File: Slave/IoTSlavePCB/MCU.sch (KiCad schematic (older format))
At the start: 12 parts

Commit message: Continued work on slaves. Added sensor and begun work on ZigBee transceiver.
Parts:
- C? (x5): footprint (none) -> Capacitor_SMD:C_0603_1608Metric
- R?: footprint (none) -> Resistor_SMD:R_0603_1608Metric
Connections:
- net JTCK: now also U?.49 (PA14)
- net JTDI: now also U?.50 (PA15)
- net JTDO: now also U?.54 (PB3)
- net JTMS: now also U?.46 (PA13)
- net NRST: now also U?.55 (PB4)
- net USART_RX: now also U?.58 (PB7)
- net USART_TX: now also U?.57 (PB6)
- net SPI1_SCK: now reaches U?.15 (PA1)
- net ~SPI1_NSS: now reaches U?.20 (PA4)
- net SPI1_MISO: now reaches U?.22 (PA6)
- net SPI1_MOSI: now reaches U?.23 (PA7)
- net I2C1_SCL: now reaches U?.42 (PA9)
- net I2C1_SDA: now reaches U?.43 (PA10)
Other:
- moved on the sheet: C?, R?
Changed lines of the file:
@@
 F 0 "C?" H 2250 2550 50  0000 L CNN
 F 1 "100 nF" H 2100 2450 50  0000 L CNN
-F 2 "" H 2538 2300 50  0001 C CNN
+F 2 "Capacitor_SMD:C_0603_1608Metric" H 2538 2300 50  0001 C CNN
 F 3 "~" H 2500 2450 50  0001 C CNN
 	1    2500 2450
@@
 	-1   0    0    1
 $EndComp
-Wire Wire Line
-	2650 3850 2150 3850
 $Comp
 L Device:C C?
 U 1 1 5F9FADD1
-P 2150 4050
-F 0 "C?" H 2150 4150 50  0000 L CNN
-F 1 "1 µF" H 2150 3950 50  0000 L CNN
-F 2 "" H 2188 3900 50  0001 C CNN
-F 3 "~" H 2150 4050 50  0001 C CNN
-	1    2150 4050
+P 2000 4050
+F 0 "C?" H 2000 4150 50  0000 L CNN
+F 1 "1 µF" H 2000 3950 50  0000 L CNN
+F 2 "" H 2038 3900 50  0001 C CNN
+F 3 "~" H 2000 4050 50  0001 C CNN
+	1    2000 4050
 	1    0    0    -1
 $EndComp
@@
 L Device:C C?
 U 1 1 5F9FB54A
-P 1950 4050
-F 0 "C?" H 1850 4150 50  0000 L CNN
-F 1 "10 nF" H 1700 3950 50  0000 L CNN
-F 2 "" H 1988 3900 50  0001 C CNN
-F 3 "~" H 1950 4050 50  0001 C CNN
-	1    1950 4050
-	1    0    0    -1
-$EndComp
-Wire Wire Line
-	2150 3850 2150 3900
-Wire Wire Line
-	2150 3850 1950 3850
-Wire Wire Line
-	1950 3850 1950 3900
-Connection ~ 2150 3850
-Connection ~ 1950 3850
+P 1800 4050
+F 0 "C?" H 1700 4150 50  0000 L CNN
+F 1 "10 nF" H 1550 3950 50  0000 L CNN
+F 2 "Capacitor_SMD:C_0603_1608Metric" H 1838 3900 50  0001 C CNN
+F 3 "~" H 1800 4050 50  0001 C CNN
+	1    1800 4050
+	1    0    0    -1
+$EndComp
+Wire Wire Line
+	2000 3850 2000 3900
+Wire Wire Line
+	1800 3850 1800 3900
 $Comp
 L Device:Ferrite_Bead_Small FB?
@@
 250 mA
 Wire Wire Line
-	1650 3850 1950 3850
+	1650 3850 1800 3850
 Wire Wire Line
 	1450 3850 1350 3850
@@
 $EndComp
 Wire Wire Line
-	1950 4200 1950 4250
-Wire Wire Line
-	1950 4250 2050 4250
-Wire Wire Line
-	2150 4250 2150 4200
+	1800 4200 1800 4250
+Wire Wire Line
+	1800 4250 1900 4250
+Wire Wire Line
+	2000 4250 2000 4200
 $Comp
 L power:GND #PWR?
 U 1 1 5F9FE7E1
-P 2050 4250
-F 0 "#PWR?" H 2050 4000 50  0001 C CNN
-F 1 "GND" H 2055 4077 50  0000 C CNN
-F 2 "" H 2050 4250 50  0001 C CNN
-F 3 "" H 2050 4250 50  0001 C CNN
-	1    2050 4250
-	1    0    0    -1
-$EndComp
-Connection ~ 2050 4250
-Wire Wire Line
-	2050 4250 2150 4250
+P 1900 4250
+F 0 "#PWR?" H 1900 4000 50  0001 C CNN
+F 1 "GND" H 1905 4077 50  0000 C CNN
+F 2 "" H 1900 4250 50  0001 C CNN
+F 3 "" H 1900 4250 50  0001 C CNN
+	1    1900 4250
+	1    0    0    -1
+$EndComp
+Connection ~ 1900 4250
+Wire Wire Line
+	1900 4250 2000 4250
 $Comp
 L Device:C C?
@@
 F 0 "C?" V 2900 5350 50  0000 L CNN
 F 1 "100 nF" V 2800 5250 50  0000 L CNN
-F 2 "" H 2988 5150 50  0001 C CNN
+F 2 "Capacitor_SMD:C_0603_1608Metric" H 2988 5150 50  0001 C CNN
 F 3 "~" H 2950 5300 50  0001 C CNN
 	1    2950 5300
@@
 F 0 "C?" V 4600 5150 50  0000 L CNN
 F 1 "100 nF" V 4500 5050 50  0000 L CNN
-F 2 "" H 4688 5150 50  0001 C CNN
+F 2 "Capacitor_SMD:C_0603_1608Metric" H 4688 5150 50  0001 C CNN
 F 3 "~" H 4650 5300 50  0001 C CNN
 	1    4650 5300
@@
 P 4450 5450
 F 0 "#PWR?" H 4450 5300 50  0001 C CNN
-F 1 "+1V8" V 4450 5600 50  0000 L CNN
+F 1 "+1V8" H 4400 5650 50  0000 L CNN
 F 2 "" H 4450 5450 50  0001 C CNN
 F 3 "" H 4450 5450 50  0001 C CNN
@@
 L power:+1V8 #PWR?
 U 1 1 5FA146ED
-P 2950 1150
-F 0 "#PWR?" H 2950 1000 50  0001 C CNN
-F 1 "+1V8" H 2850 1350 50  0000 L CNN
-F 2 "" H 2950 1150 50  0001 C CNN
-F 3 "" H 2950 1150 50  0001 C CNN
-	1    2950 1150
+P 2950 1000
+F 0 "#PWR?" H 2950 850 50  0001 C CNN
+F 1 "+1V8" H 2850 1150 50  0000 L CNN
+F 2 "" H 2950 1000 50  0001 C CNN
+F 3 "" H 2950 1000 50  0001 C CNN
+	1    2950 1000
 	1    0    0    -1
 $EndComp
@@
 $EndComp
 Wire Wire Line
-	2950 1150 2950 1300
-Wire Wire Line
 	2950 1300 2900 1300
 Connection ~ 2950 1300
@@
 F 0 "C?" H 4950 2400 50  0000 L CNN
 F 1 "100 nF" H 4750 2500 50  0000 L CNN
-F 2 "" H 5188 2300 50  0001 C CNN
+F 2 "Capacitor_SMD:C_0603_1608Metric" H 5188 2300 50  0001 C CNN
 F 3 "~" H 5150 2450 50  0001 C CNN
 	1    5150 2450
@@
 L Device:R R?
 U 1 1 5FA1DB71
-P 3450 1500
-F 0 "R?" H 3450 1650 50  0000 L CNN
-F 1 "4.7k" V 3450 1400 50  0000 L CNN
-F 2 "" V 3380 1500 50  0001 C CNN
-F 3 "~" H 3450 1500 50  0001 C CNN
-	1    3450 1500
-	1    0    0    -1
-$EndComp
-Wire Wire Line
-	3450 1350 3450 1300
+P 3450 1200
+F 0 "R?" H 3300 1200 50  0000 L CNN
+F 1 "4.7k" V 3450 1100 50  0000 L CNN
+F 2 "Resistor_SMD:R_0603_1608Metric" V 3380 1200 50  0001 C CNN
+F 3 "~" H 3450 1200 50  0001 C CNN
+	1    3450 1200
+	1    0    0    -1
+$EndComp
+Wire Wire Line
+	3450 1050 3450 1000
 $Comp
 L power:GND #PWR?
 U 1 1 5FA1EB69
-P 3450 1300
-F 0 "#PWR?" H 3450 1050 50  0001 C CNN
-F 1 "GND" H 3450 1150 50  0000 C CNN
-F 2 "" H 3450 1300 50  0001 C CNN
-F 3 "" H 3450 1300 50  0001 C CNN
-	1    3450 1300
-	-1   0    0    1
-$EndComp
-Wire Wire Line
-	3450 1650 3450 1750
+P 3450 1000
+F 0 "#PWR?" H 3450 750 50  0001 C CNN
+F 1 "GND" H 3450 850 50  0000 C CNN
+F 2 "" H 3450 1000 50  0001 C CNN
+F 3 "" H 3450 1000 50  0001 C CNN
+	1    3450 1000
+	-1   0    0    1
+$EndComp
 $Comp
 L Connector_Generic:Conn_02x07_Odd_Even J?
@@
 Wire Wire Line
 	3150 1750 3150 1700
+Text Label 3850 1700 1    50   ~ 0
+NRST
+Wire Wire Line
+	3850 1750 3850 1700
+Text Label 4800 2850 0    50   ~ 0
+JTMS
+Text Label 4450 1700 1    50   ~ 0
+JTCK
+Text Label 3950 1700 1    50   ~ 0
+JTDO
+Text Label 4350 1700 1    50   ~ 0
+JTDI
+Wire Wire Line
+	3950 1700 3950 1750
+Wire Wire Line
+	4800 2850 4750 2850
+Wire Wire Line
+	4450 1700 4450 1750
+Wire Wire Line
+	4350 1700 4350 1750
+Text Label 3550 1700 1    50   ~ 0
+USART_RX
+Text Label 3650 1700 1    50   ~ 0
+USART_TX
+Wire Wire Line
+	3550 1700 3550 1750
+Wire Wire Line
+	3650 1700 3650 1750
+Wire Wire Line
+	3450 1350 3450 1750
+Wire Wire Line
+	2950 1000 2950 1300
+Wire Wire Line
+	4800 3150 4750 3150
+Wire Wire Line
+	4750 3250 4800 3250
+Text HLabel 4800 3250 2    50   Output ~ 0
+I2C1_SCL
+Text HLabel 4800 3150 2    50   BiDi ~ 0
+I2C1_SDA
+Wire Wire Line
+	2650 4050 2600 4050
+Wire Wire Line
+	3250 4850 3250 4900
+Wire Wire Line
+	3450 4850 3450 4900
+Wire Wire Line
+	3550 4850 3550 4900
+Text HLabel 2600 4050 0    50   Output ~ 0
+SPI1_SCK
+Connection ~ 1800 3850
+Connection ~ 2000 3850
+Wire Wire Line
+	2000 3850 2650 3850
+Wire Wire Line
+	1800 3850 2000 3850
+Text HLabel 3250 4900 3    50   Output ~ 0
+~SPI1_NSS
+Text HLabel 3450 4900 3    50   Input ~ 0
+SPI1_MISO
+Text HLabel 3550 4900 3    50   Output ~ 0
+SPI1_MOSI
 $EndSCHEMATC

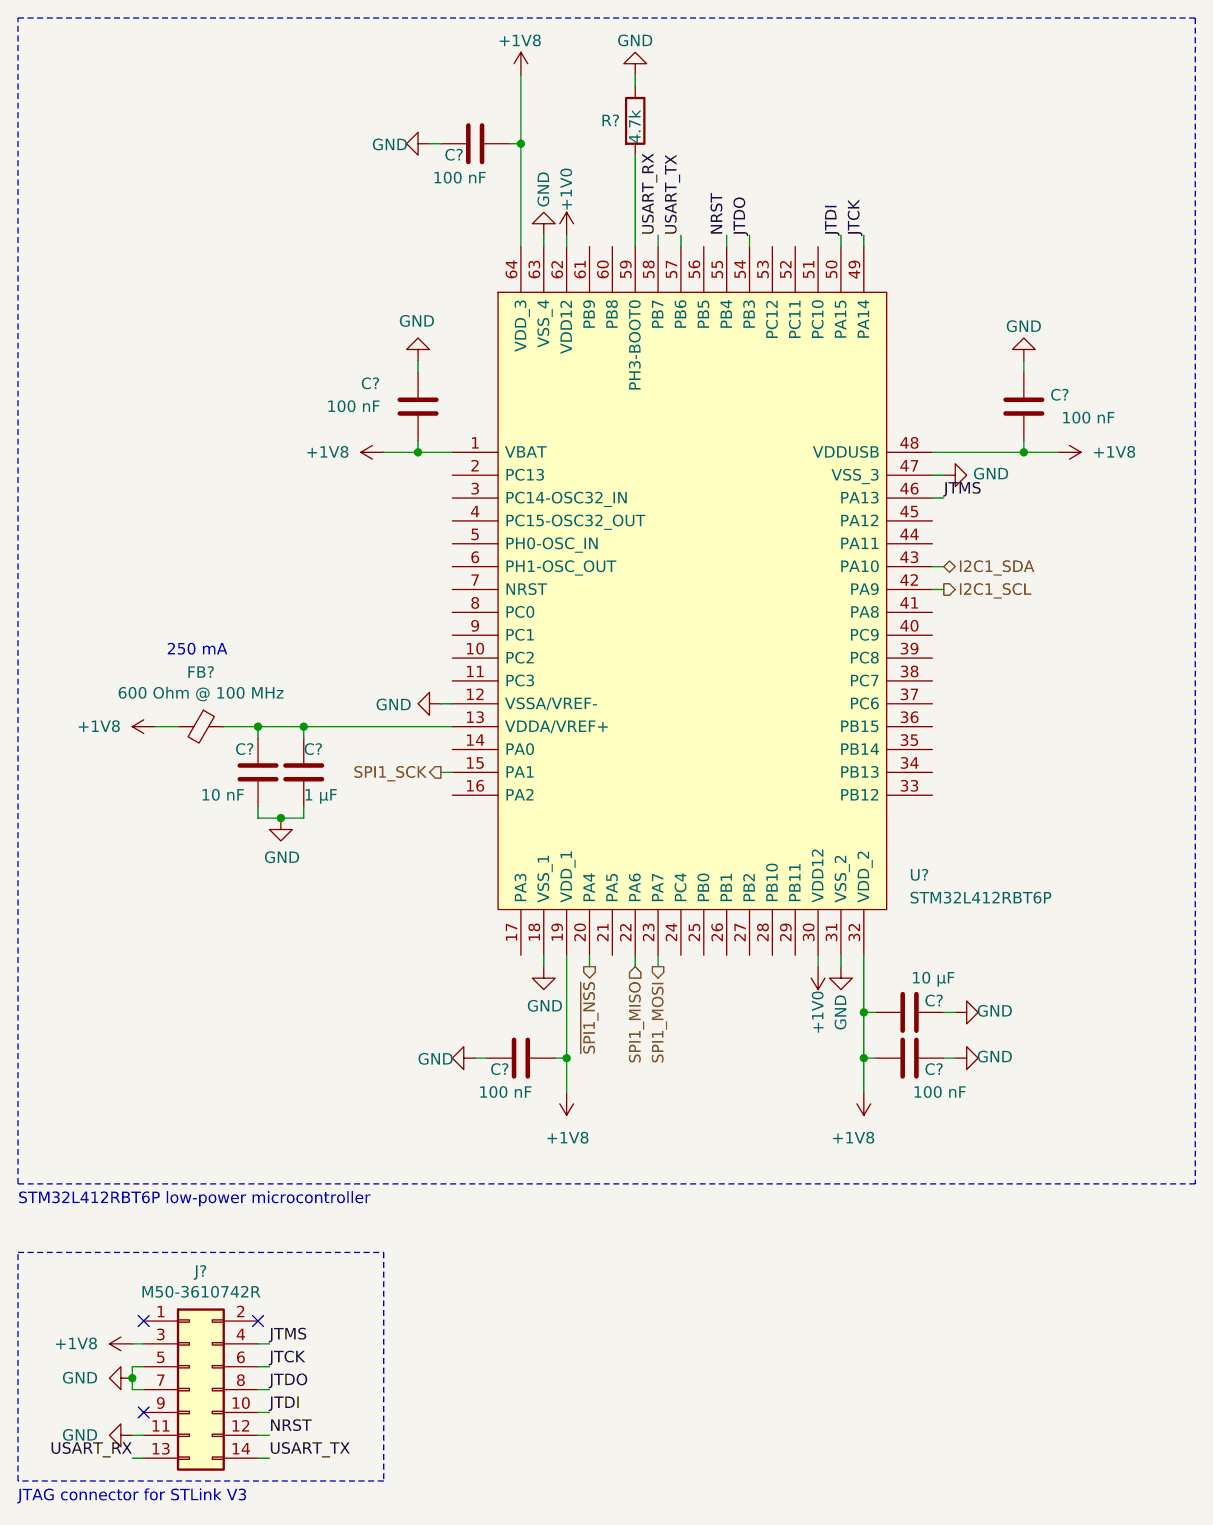
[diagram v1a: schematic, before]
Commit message: Finished slave schematics, including memory and Zigbee Transceiver. Further work on PCB, well underway.
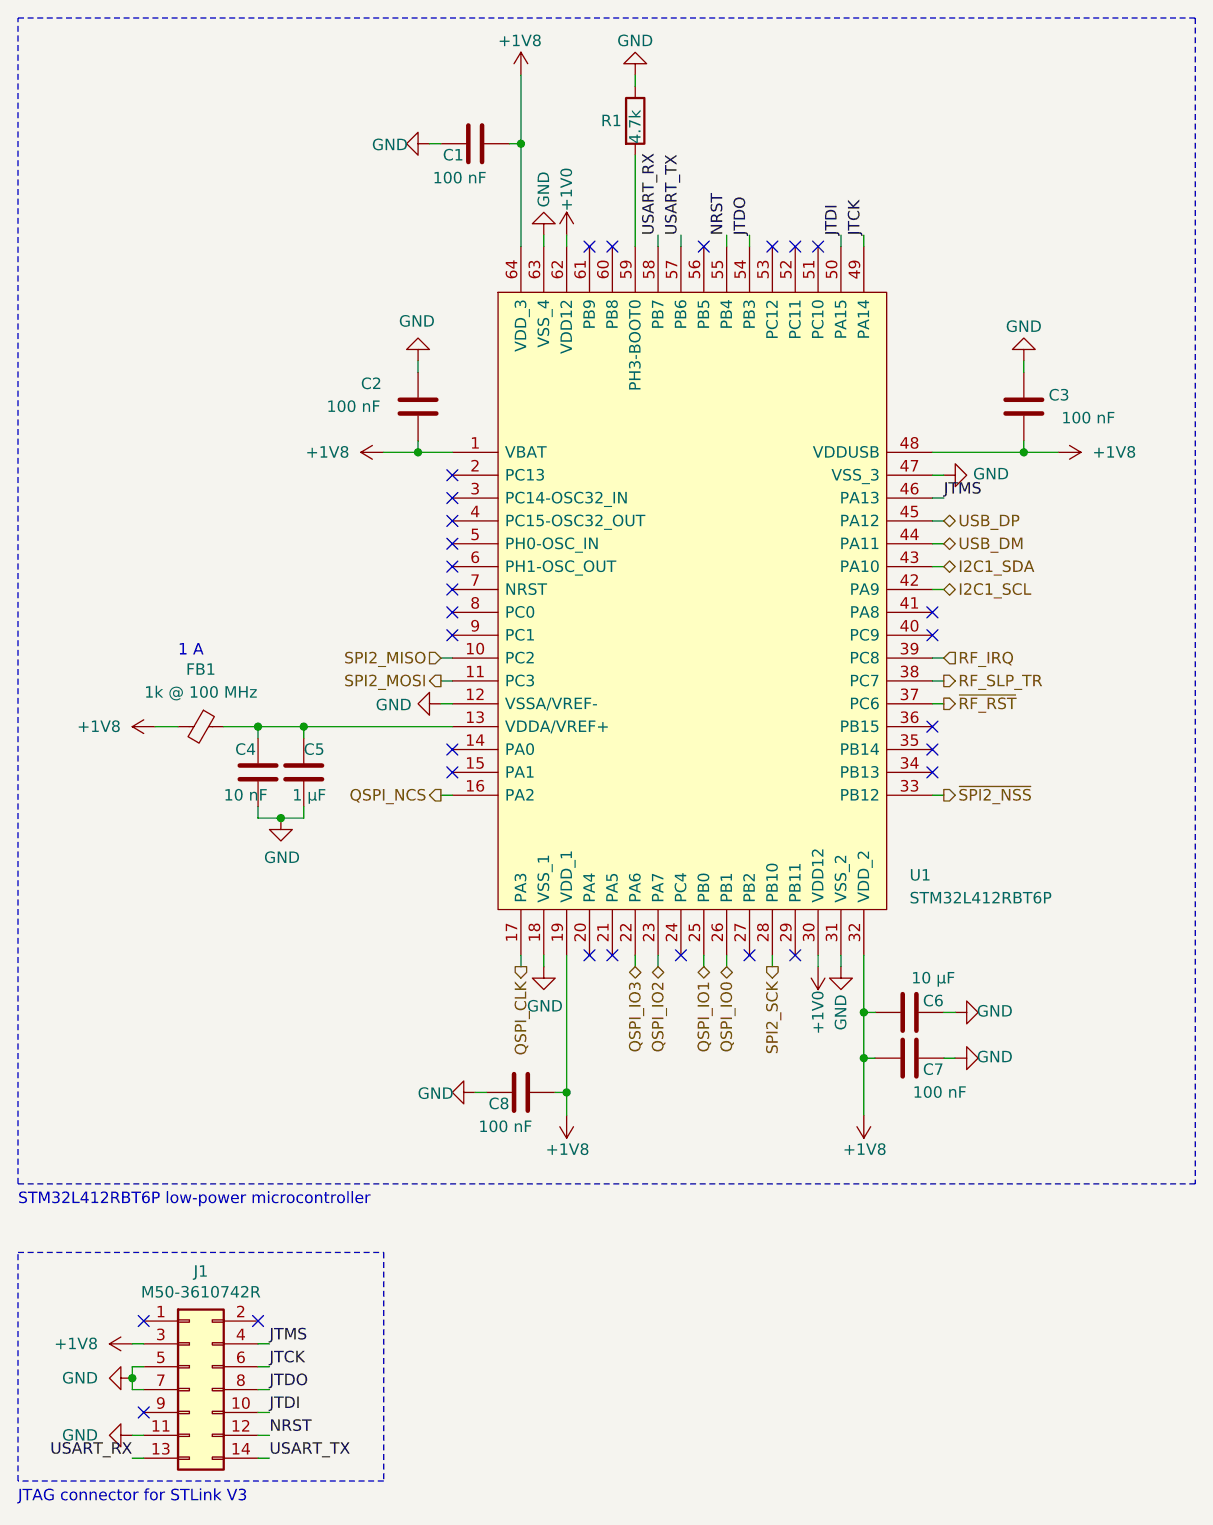
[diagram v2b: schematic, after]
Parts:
- removed FB?: 600 Ohm @ 100 MHz, symbol Device:Ferrite_Bead_Small
- added FB1: 1k @ 100 MHz, Inductor_SMD:L_0603_1608Metric, symbol Device:Ferrite_Bead_Small
- C1: renamed from C?; footprint (none) -> Capacitor_SMD:C_0603_1608Metric
- C5, C6: renamed from C?; footprint (none) -> Capacitor_SMD:C_0805_2012Metric
- gave numbers to parts that had none: 8
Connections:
- net +1V8: now also FB1.2
- net SPI2_MISO: now reaches U1.10 (PC2)
- net SPI2_MOSI: now reaches U1.11 (PC3)
- net at C4.1, C5.1, U1.13 (VDDA/VREF+): now also FB1.1
- net QSPI_NCS: now reaches U1.16 (PA2)
- net QSPI_CLK: now reaches U1.17 (PA3)
- net QSPI_IO1: now reaches U1.25 (PB0)
- net QSPI_IO0: now reaches U1.26 (PB1)
- net SPI2_SCK: now reaches U1.28 (PB10)
- net ~SPI2_NSS: now reaches U1.33 (PB12)
- net ~RF_RST: now reaches U1.37 (PC6)
- net RF_SLP_TR: now reaches U1.38 (PC7)
- net RF_IRQ: now reaches U1.39 (PC8)
- net USB_DM: now reaches U1.44 (PA11)
- net USB_DP: now reaches U1.45 (PA12)
- net SPI1_MISO renamed QSPI_IO3
- net SPI1_MOSI renamed QSPI_IO2
- net SPI1_SCK: no longer names the net of U1.15 (PA1)
- net ~SPI1_NSS: no longer names the net of U1.20 (PA4)
- no-connect marks 3 -> 29
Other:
- note added: "1 A"
- note removed: "250 mA"
- moved on the sheet: C8

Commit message: Made more connections on PCB, some optimizations. Added silk screen text.
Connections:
- net USB_DM renamed USB_DN
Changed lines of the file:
@@
 USB_DP
 Text HLabel 4800 3050 2    50   BiDi ~ 0
-USB_DM
+USB_DN
 Text HLabel 2600 4150 0    50   Output ~ 0
 QSPI_NCS

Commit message: Added battery voltage measurement circuit. Optimizations to antenna and general component placement.
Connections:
- net ADC_Battery: now reaches U1.8 (PC0)
- no-connect marks 29 -> 28
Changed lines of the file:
@@
 NoConn ~ 2650 3150
 NoConn ~ 2650 3250
-NoConn ~ 2650 3350
 NoConn ~ 2650 3450
 NoConn ~ 2650 3950
@@
 Text Notes 1450 3550 0    50   ~ 0
 1 A
+Text HLabel 2600 3350 0    50   Input ~ 0
+ADC_Battery
+Wire Wire Line
+	2650 3350 2600 3350
 $EndSCHEMATC
